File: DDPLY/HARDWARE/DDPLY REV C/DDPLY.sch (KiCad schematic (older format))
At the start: 34 parts, among them P1 USB_OTG, P2 PWR, P3 SW, P4 E-MATCH_1, P5 ICSP, P6 E-MATCH_2, P7 PIEZO, Q1 Q_NJFET_GSD, Q2 Q_NJFET_GSD, Q3 Q_NJFET_GSD, U1 AP2210, U2 FT230XQ-R, U4 BMP280, U5 ATTINY841-MMH

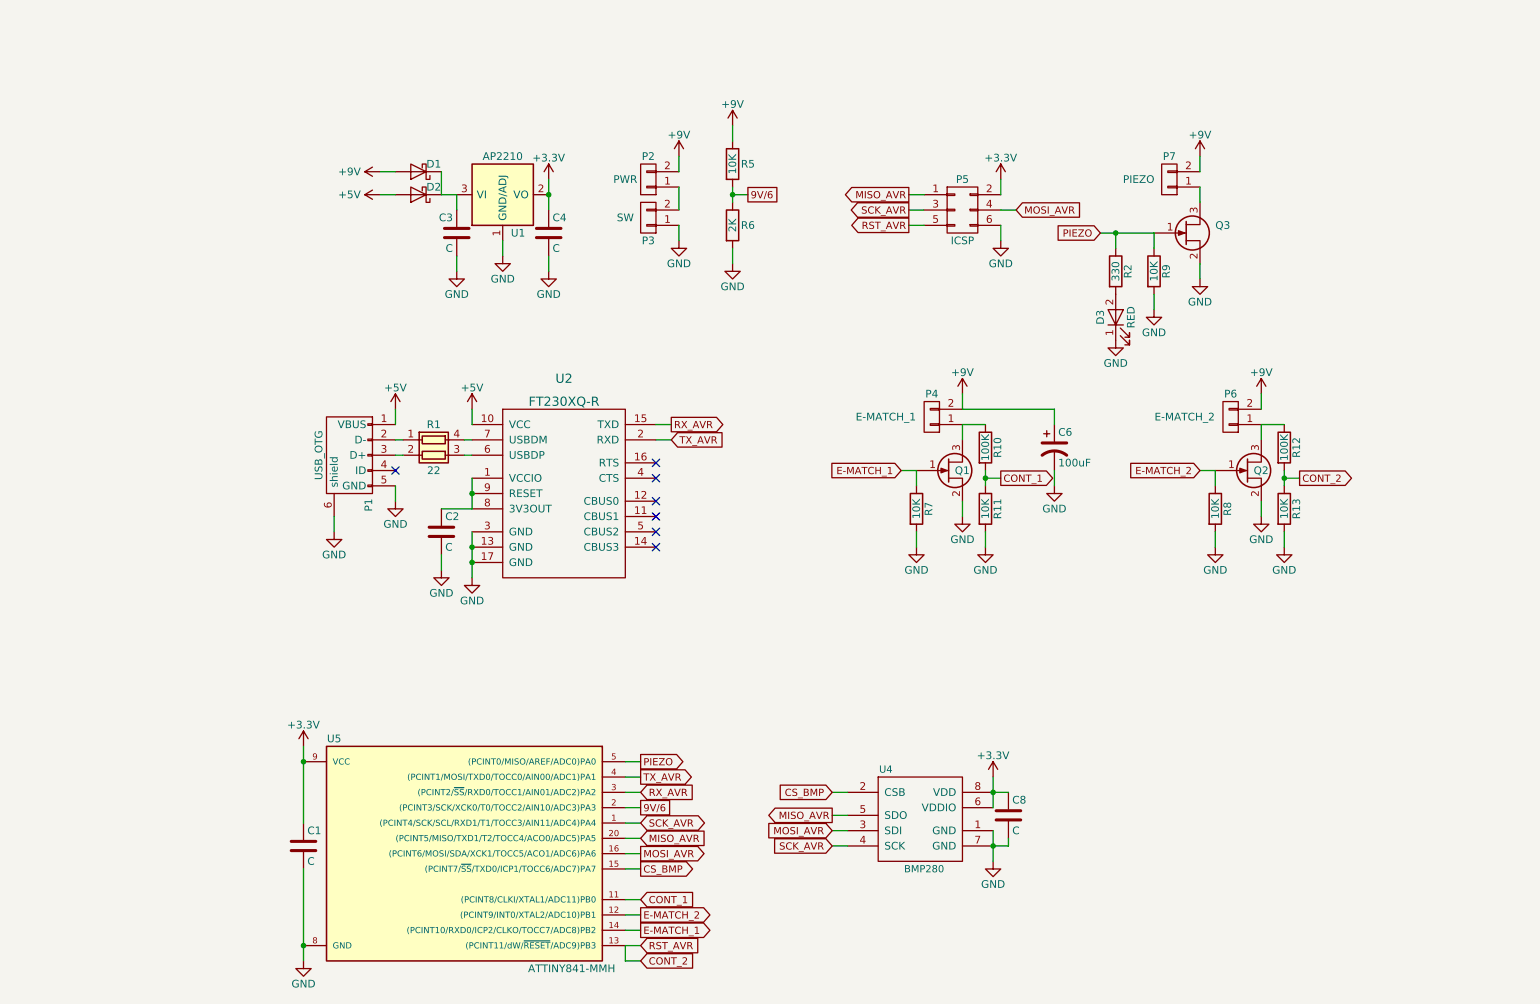
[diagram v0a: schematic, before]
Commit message: fixed pin 1 dot on LWRA, firmware folder renamed
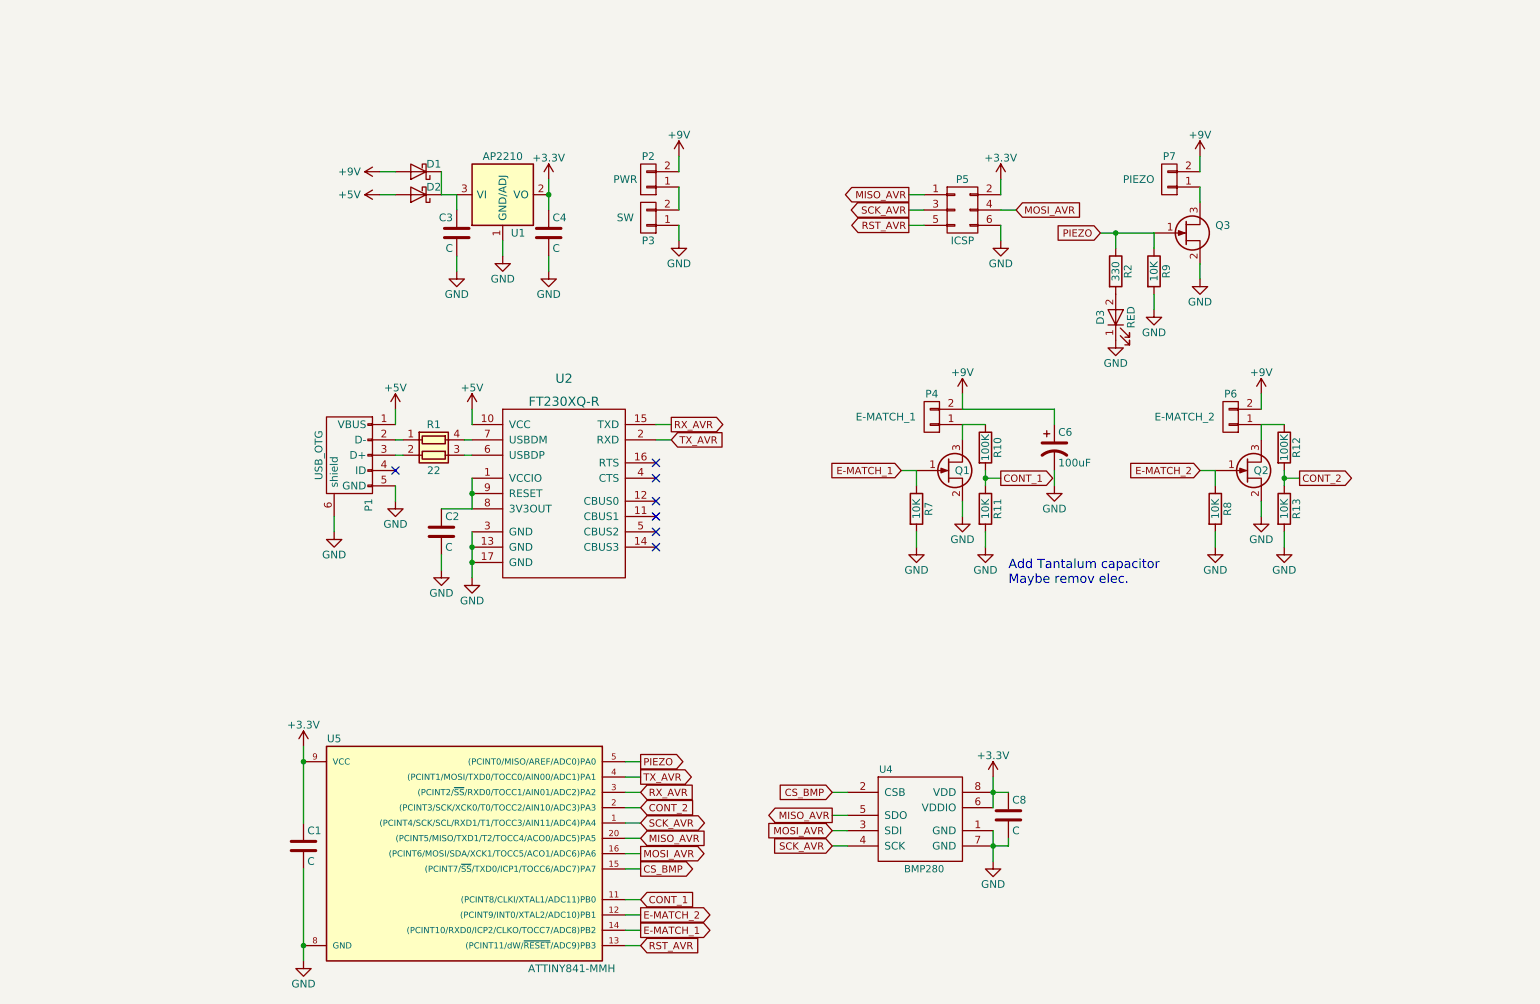
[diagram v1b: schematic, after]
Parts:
- removed R5: 10K, Resistors_SMD:R_0603, symbol R
- removed R6: 2K, Resistors_SMD:R_0603, symbol R
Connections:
- net 9V/6 is gone; now on net CONT_2: U5.2 ((PCINT3/SCK/XCK0/T0/TOCC2/AIN10/ADC3)PA3)
- net CONT_2: no longer P5.5 (P5), U5.13 ((PCINT11/dW/~RESET~/ADC9)PB3)
- new net RST_AVR: P5.5 (P5), U5.13 ((PCINT11/dW/~RESET~/ADC9)PB3)
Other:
- note added: "Add Tantalum capacitor\nMaybe remov elec.\n"
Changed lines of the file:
@@
 Wire Wire Line
 	5400 5500 5500 5500
-Text GLabel 5500 5600 2    47   UnSpc ~ 0
-9V/6
-Wire Wire Line
-	5500 5600 5400 5600
-$Comp
-L R R5
-U 1 1 59DAE6E8
-P 6100 1400
-F 0 "R5" H 6200 1400 50  0000 C CNN
-F 1 "10K" V 6100 1400 50  0000 C CNN
-F 2 "Resistors_SMD:R_0603" V 6030 1400 50  0001 C CNN
-F 3 "" H 6100 1400 50  0000 C CNN
-	1    6100 1400
-	1    0    0    -1
-$EndComp
-$Comp
-L R R6
-U 1 1 59DAE74D
-P 6100 1800
-F 0 "R6" H 6200 1800 50  0000 C CNN
-F 1 "2K" V 6100 1800 50  0000 C CNN
-F 2 "Resistors_SMD:R_0603" V 6030 1800 50  0001 C CNN
-F 3 "" H 6100 1800 50  0000 C CNN
-	1    6100 1800
-	1    0    0    -1
-$EndComp
-$Comp
-L +9V #PWR028
-U 1 1 59DAE7B2
-P 6100 1150
-F 0 "#PWR028" H 6100 1000 50  0001 C CNN
-F 1 "+9V" H 6100 1290 50  0000 C CNN
-F 2 "" H 6100 1150 50  0000 C CNN
-F 3 "" H 6100 1150 50  0000 C CNN
-	1    6100 1150
-	1    0    0    -1
-$EndComp
-Wire Wire Line
-	6100 1150 6100 1250
-Wire Wire Line
-	6100 1550 6100 1650
-$Comp
-L GND #PWR029
-U 1 1 59DAEB68
-P 6100 2050
-F 0 "#PWR029" H 6100 1800 50  0001 C CNN
-F 1 "GND" H 6100 1900 50  0000 C CNN
-F 2 "" H 6100 2050 50  0000 C CNN
-F 3 "" H 6100 2050 50  0000 C CNN
-	1    6100 2050
-	1    0    0    -1
-$EndComp
-Wire Wire Line
-	6100 2050 6100 1950
-Text GLabel 6200 1600 2    47   UnSpc ~ 0
-9V/6
-Wire Wire Line
-	6200 1600 6100 1600
-Connection ~ 6100 1600
 Text GLabel 5500 6400 2    47   Output ~ 0
 E-MATCH_1
@@
 Text GLabel 5500 6200 2    47   Input ~ 0
 CONT_1
-Text GLabel 5500 6600 2    47   Input ~ 0
+Text GLabel 5500 5600 2    47   Input ~ 0
 CONT_2
 Wire Wire Line
 	5500 6200 5400 6200
 Wire Wire Line
-	5500 6600 5400 6600
-Wire Wire Line
-	5400 6600 5400 6500
+	5500 5600 5400 5600
 Text GLabel 7850 3450 2    47   Output ~ 0
 CONT_1
@@
 	8600 1950 8600 1850
 Connection ~ 8600 1850
+Text Notes 7900 4150 0    60   ~ 0
+Add Tantalum capacitor\nMaybe remov elec.\n
 $EndSCHEMATC

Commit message: LWRA BOM fix
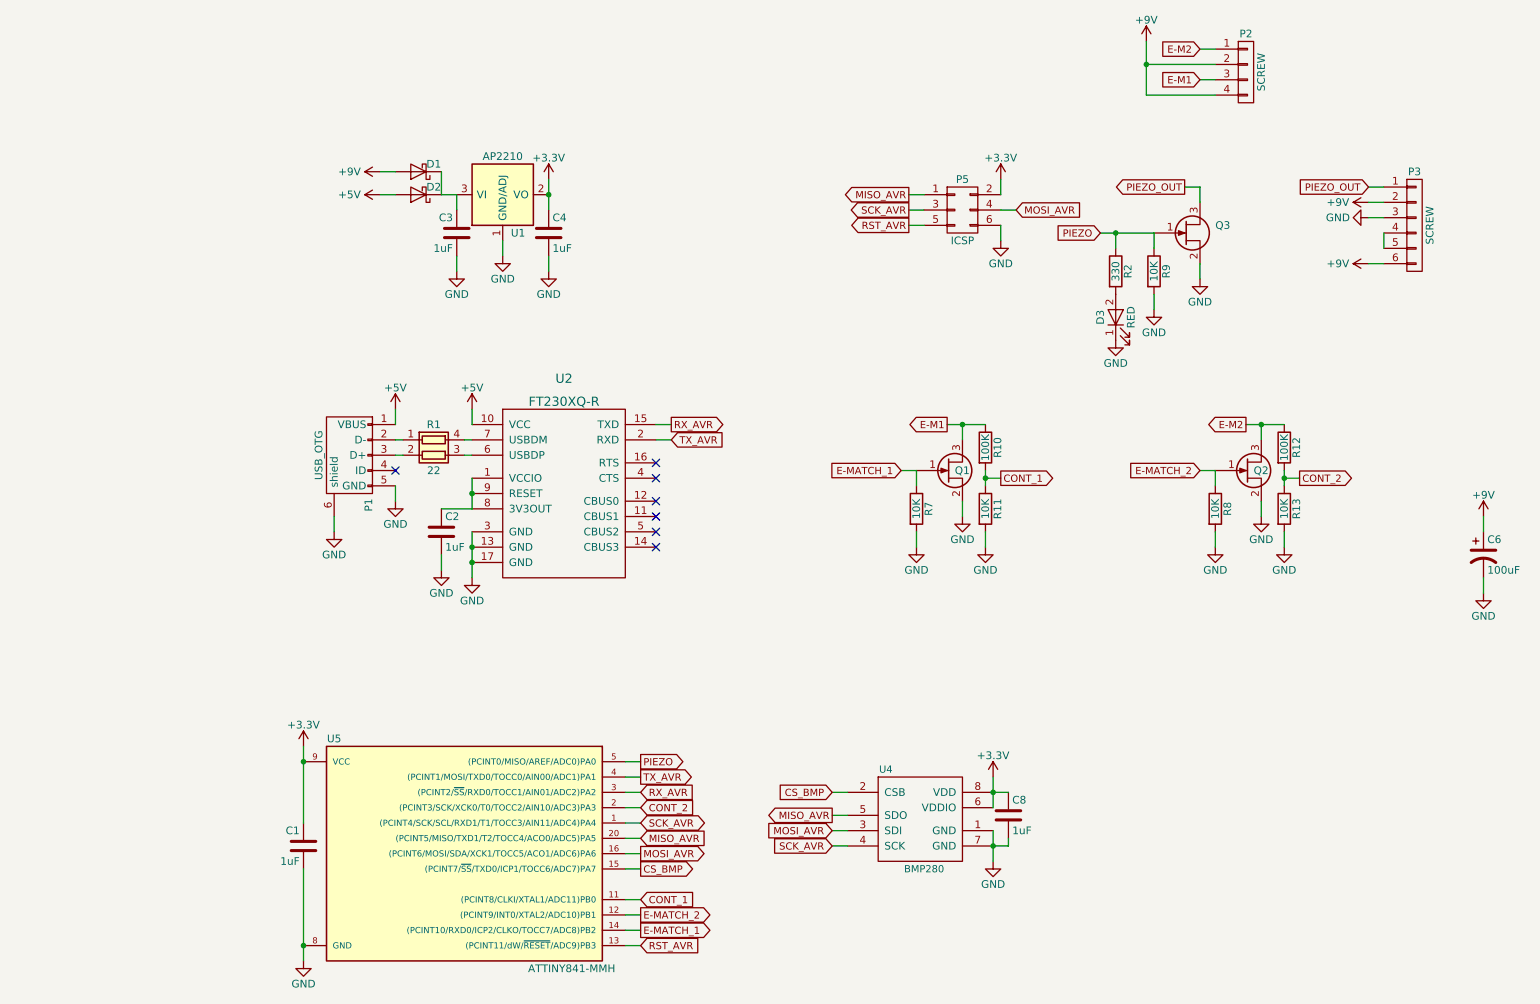
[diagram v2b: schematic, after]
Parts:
- removed P2: PWR, MOD:100MIL_ST, symbol CONN_01X02
- removed P3: SW, MOD:100MIL_ST, symbol CONN_01X02
- removed P4: E-MATCH_1, MOD:100MIL_ST, symbol CONN_01X02
- removed P6: E-MATCH_2, MOD:100MIL_ST, symbol CONN_01X02
- removed P7: PIEZO, MOD:100MIL_ST, symbol CONN_01X02
- added P2: SCREW, MOD:100MIL_STX4, symbol CONN_01X04
- added P3: SCREW, MOD:100MIL_STX6, symbol CONN_01X06
- C1, C2, C3, C4, C8: value C -> 1uF
- C6: footprint Capacitors_SMD:CP_Elec_5x5.3 -> Capacitors_Tantalum_SMD:Tantalum_Case-B_EIA-3528-21_Reflow
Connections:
- net +9V: now also P2.2 (P2), P2.4 (P4), P3.2 (P2), P3.6 (P6)
- net GND: now also P3.3 (P3)
- net E-M1: now reaches Q1.3 (D), R10.1
- net E-M1: now also P2.3 (P3)
- net E-M2: now reaches Q2.3 (D), R12.1
- net E-M2: now also P2.1 (P1)
- net PIEZO_OUT: now reaches Q3.3 (D)
- net PIEZO_OUT: now also P3.1 (P1)
- new net: P3.4 (P4), P3.5 (P5)
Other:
- note removed: "Add Tantalum capacitor\nMaybe remov elec.\n"
- moved on the sheet: C6

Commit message: added gate resistors DDPLY
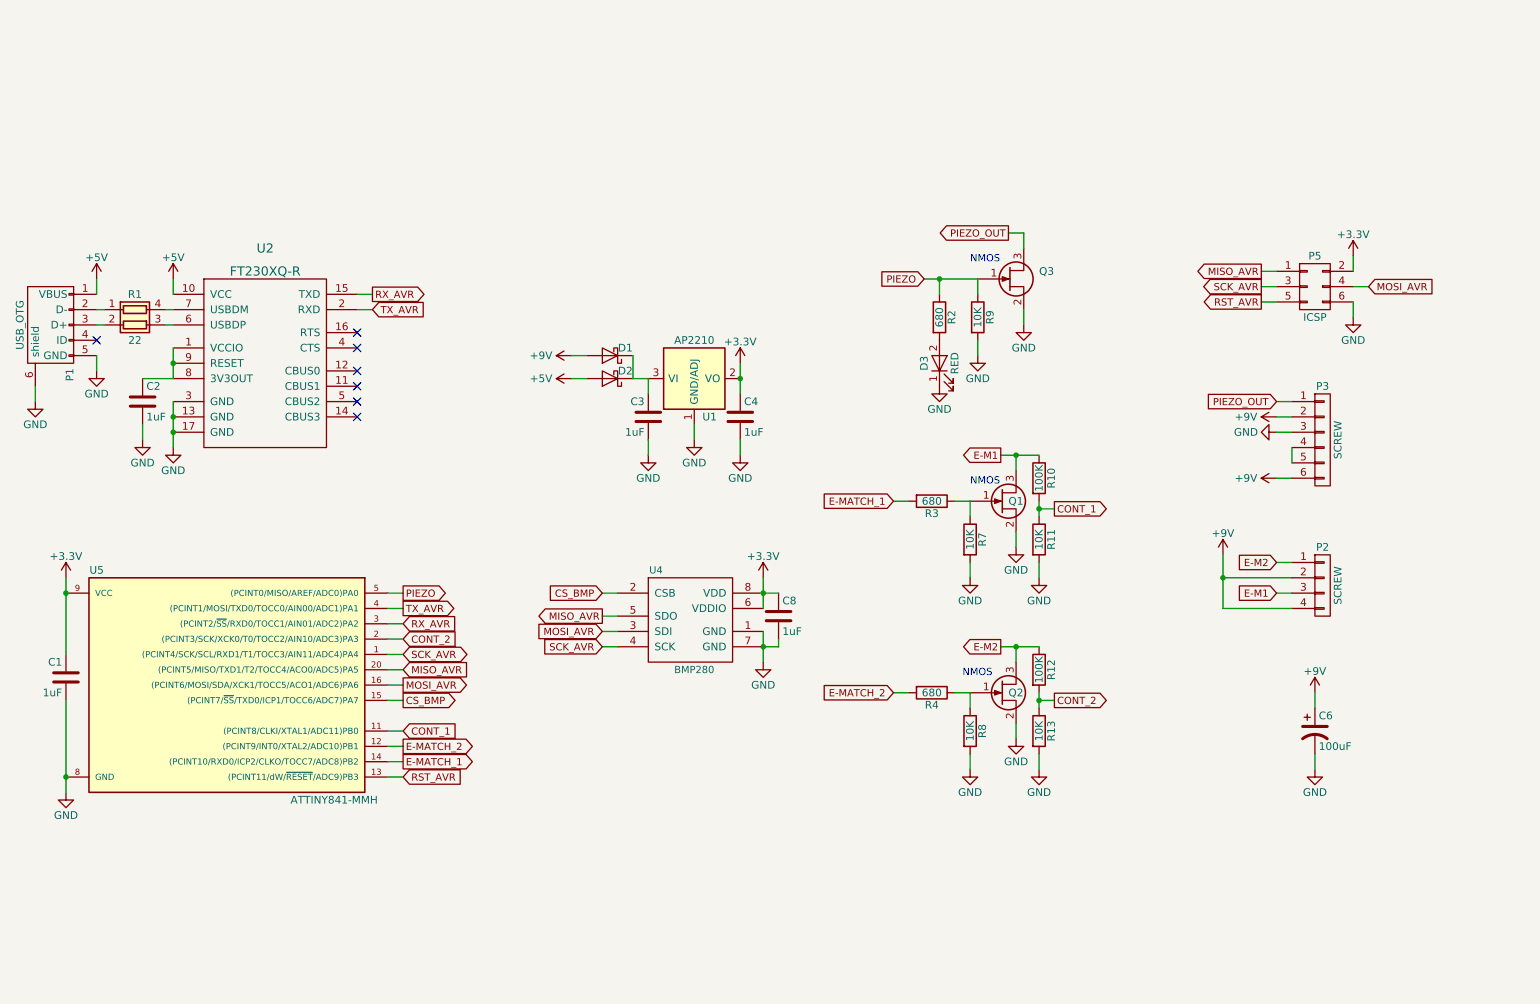
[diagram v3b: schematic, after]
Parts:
- added R3, R4: 680, Resistors_SMD:R_0603, symbol R
- R2: value 330 -> 680
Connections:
- net E-MATCH_1: now also R3.2; no longer Q1.1 (G), R7.1
- net E-MATCH_2: now also R4.2; no longer Q2.1 (G), R8.1
- new net: Q1.1 (G), R3.1, R7.1
- new net: Q2.1 (G), R4.1, R8.1
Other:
- note added: "NMOS"
- moved on the sheet: C1, C2, C3, C4, C6, C8, D1, D2, D3, P1, P2, P3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
